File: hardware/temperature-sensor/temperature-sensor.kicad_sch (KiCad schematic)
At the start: 0 parts

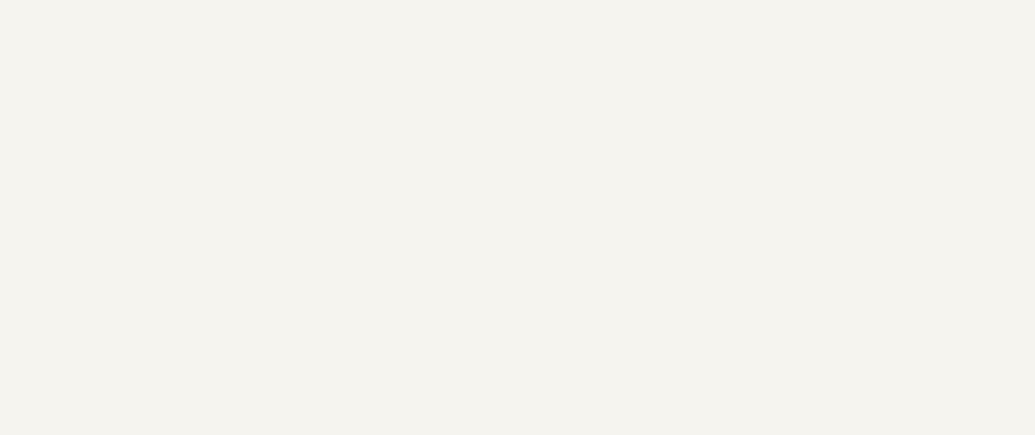
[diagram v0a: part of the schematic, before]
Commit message: extend schematic of ethernet
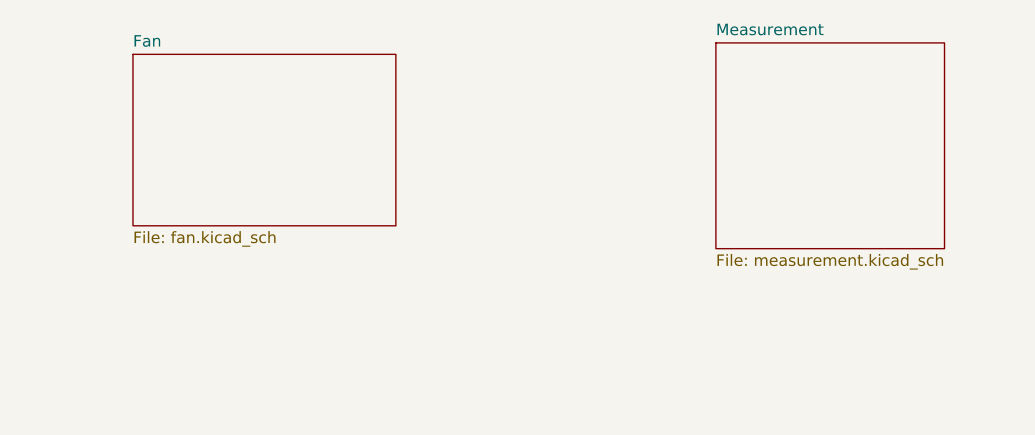
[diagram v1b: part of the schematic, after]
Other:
- added sheet Fan (fan.kicad_sch)
- added sheet Measurement (measurement.kicad_sch)
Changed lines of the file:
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@@
 	(paper "A4")
+	(sheet
+		(at 130.81 53.34)
+		(size 29.21 19.05)
+		(fields_autoplaced yes)
+		(stroke
+			(width 0.1524)
+			(type solid)
+		)
+		(fill
+			(color 0 0 0 0.0000)
+		)
+		(property "Sheetname" "Fan"
+			(at 130.81 52.6284 0)
+			(effects
+				(font
+					(size 1.27 1.27)
+				)
+				(justify left bottom)
+			)
+		)
+		(property "Sheetfile" "fan.kicad_sch"
+			(at 130.81 72.9746 0)
+			(effects
+				(font
+					(size 1.27 1.27)
+				)
+				(justify left top)
+			)
+		)
+		(instances
+			(project "temperature-sensor"
+				(path "/3594a937-0ff5-42e2-8a8f-f816088f7574"
+					(page "4")
+				)
+			)
+		)
+	)
+	(sheet
+		(at 195.58 52.07)
+		(size 25.4 22.86)
+		(fields_autoplaced yes)
+		(stroke
+			(width 0.1524)
+			(type solid)
+		)
+		(fill
+			(color 0 0 0 0.0000)
+		)
+		(property "Sheetname" "Measurement"
+			(at 195.58 51.3584 0)
+			(effects
+				(font
+					(size 1.27 1.27)
+				)
+				(justify left bottom)
+			)
+		)
+		(property "Sheetfile" "measurement.kicad_sch"
+			(at 195.58 75.5146 0)
+			(effects
+				(font
+					(size 1.27 1.27)
+				)
+				(justify left top)
+			)
+		)
+		(instances
+			(project "temperature-sensor"
+				(path "/3594a937-0ff5-42e2-8a8f-f816088f7574"
+					(page "5")
+				)
+			)
+		)
+	)
 	(sheet
 		(at 118.11 106.68)

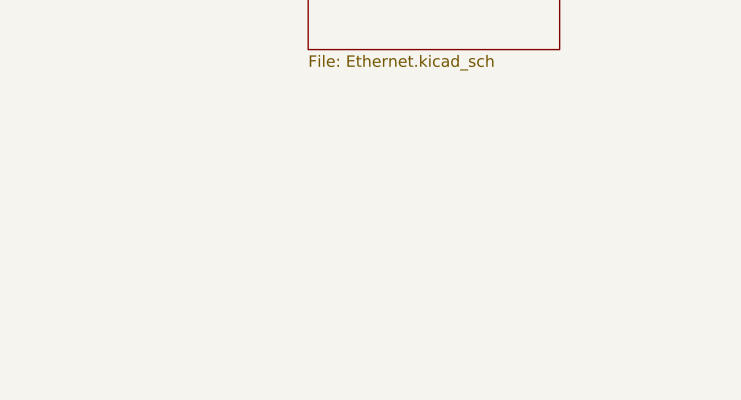
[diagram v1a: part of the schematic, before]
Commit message: replace lan transformer with a 2 channel version
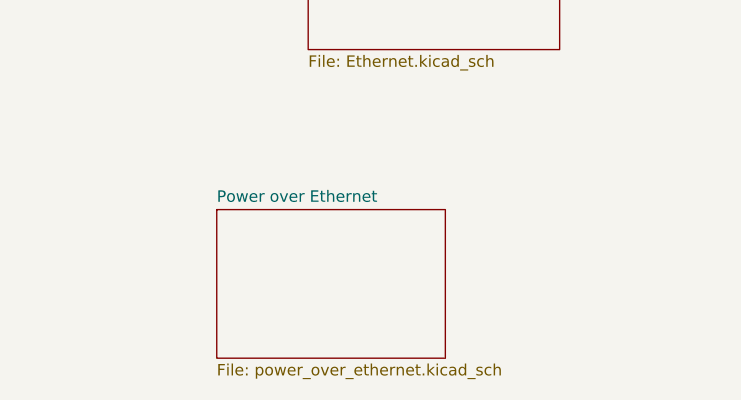
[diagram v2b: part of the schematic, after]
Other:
- added sheet Power over Ethernet (power_over_ethernet.kicad_sch)
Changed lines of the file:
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@@
+	)
+	(sheet
+		(at 172.72 134.62)
+		(size 25.4 16.51)
+		(fields_autoplaced yes)
+		(stroke
+			(width 0.1524)
+			(type solid)
+		)
+		(fill
+			(color 0 0 0 0.0000)
+		)
+		(property "Sheetname" "Power over Ethernet"
+			(at 172.72 133.9084 0)
+			(effects
+				(font
+					(size 1.27 1.27)
+				)
+				(justify left bottom)
+			)
+		)
+		(property "Sheetfile" "power_over_ethernet.kicad_sch"
+			(at 172.72 151.7146 0)
+			(effects
+				(font
+					(size 1.27 1.27)
+				)
+				(justify left top)
+			)
+		)
+		(instances
+			(project "temperature-sensor"
+				(path "/3594a937-0ff5-42e2-8a8f-f816088f7574"
+					(page "6")
+				)
+			)
+		)
 	)
 	(sheet

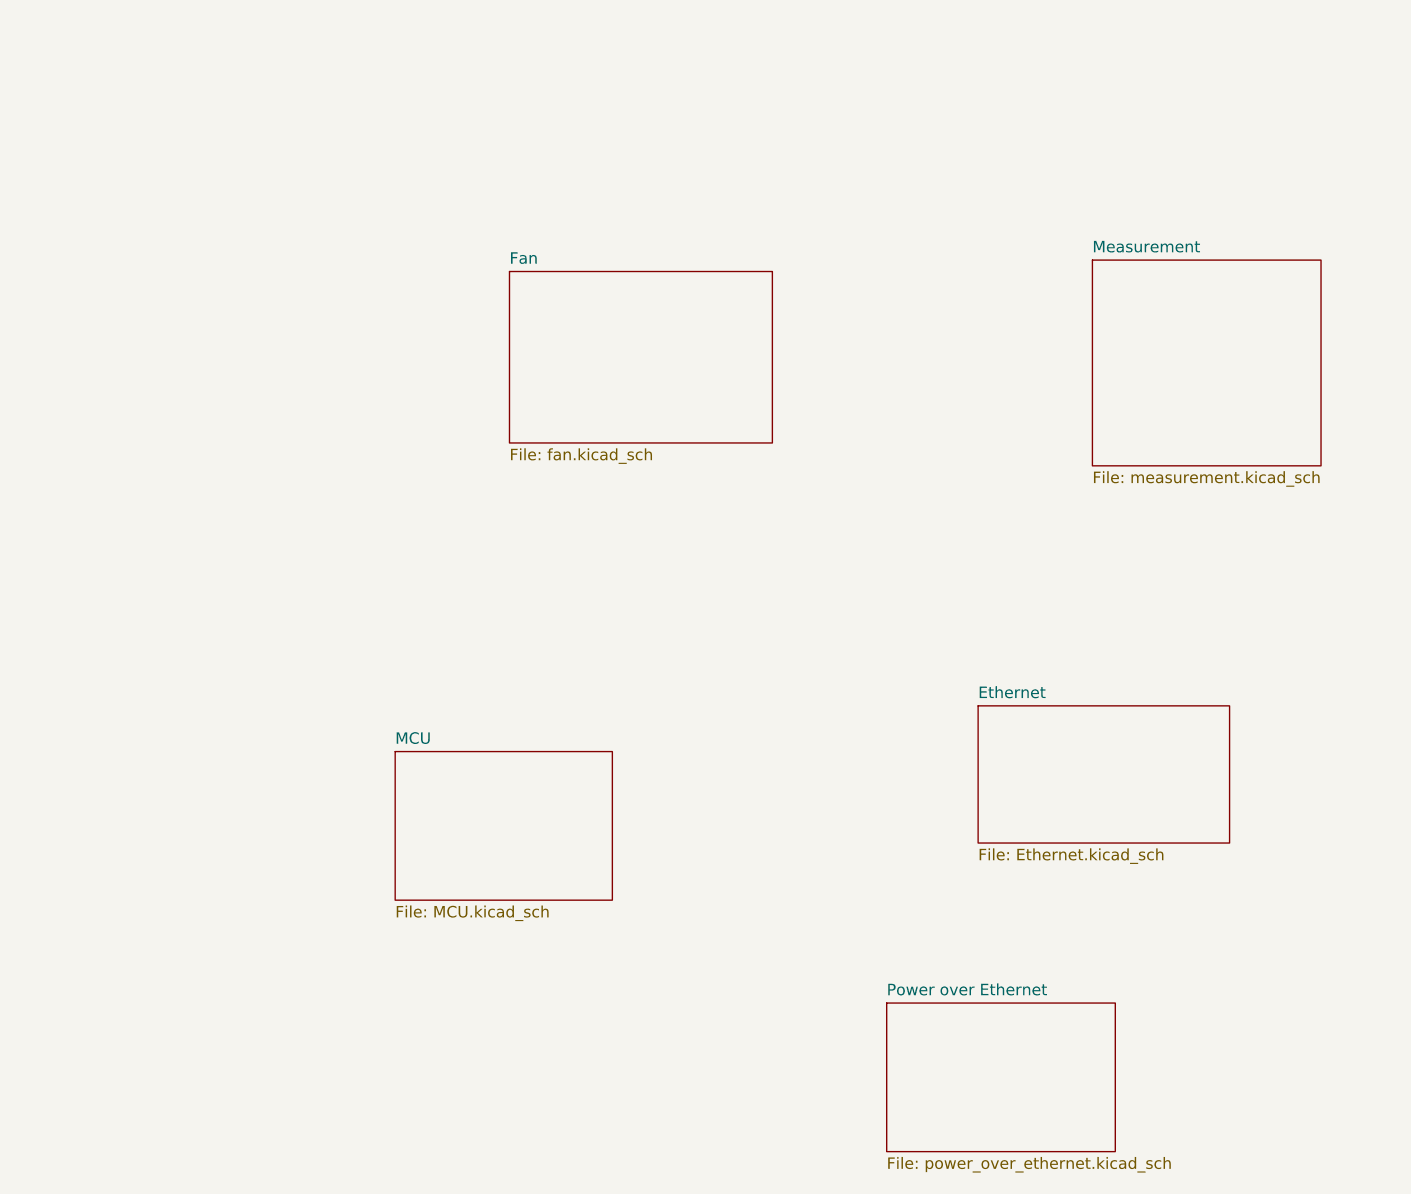
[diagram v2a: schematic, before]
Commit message: work on temperature sensor
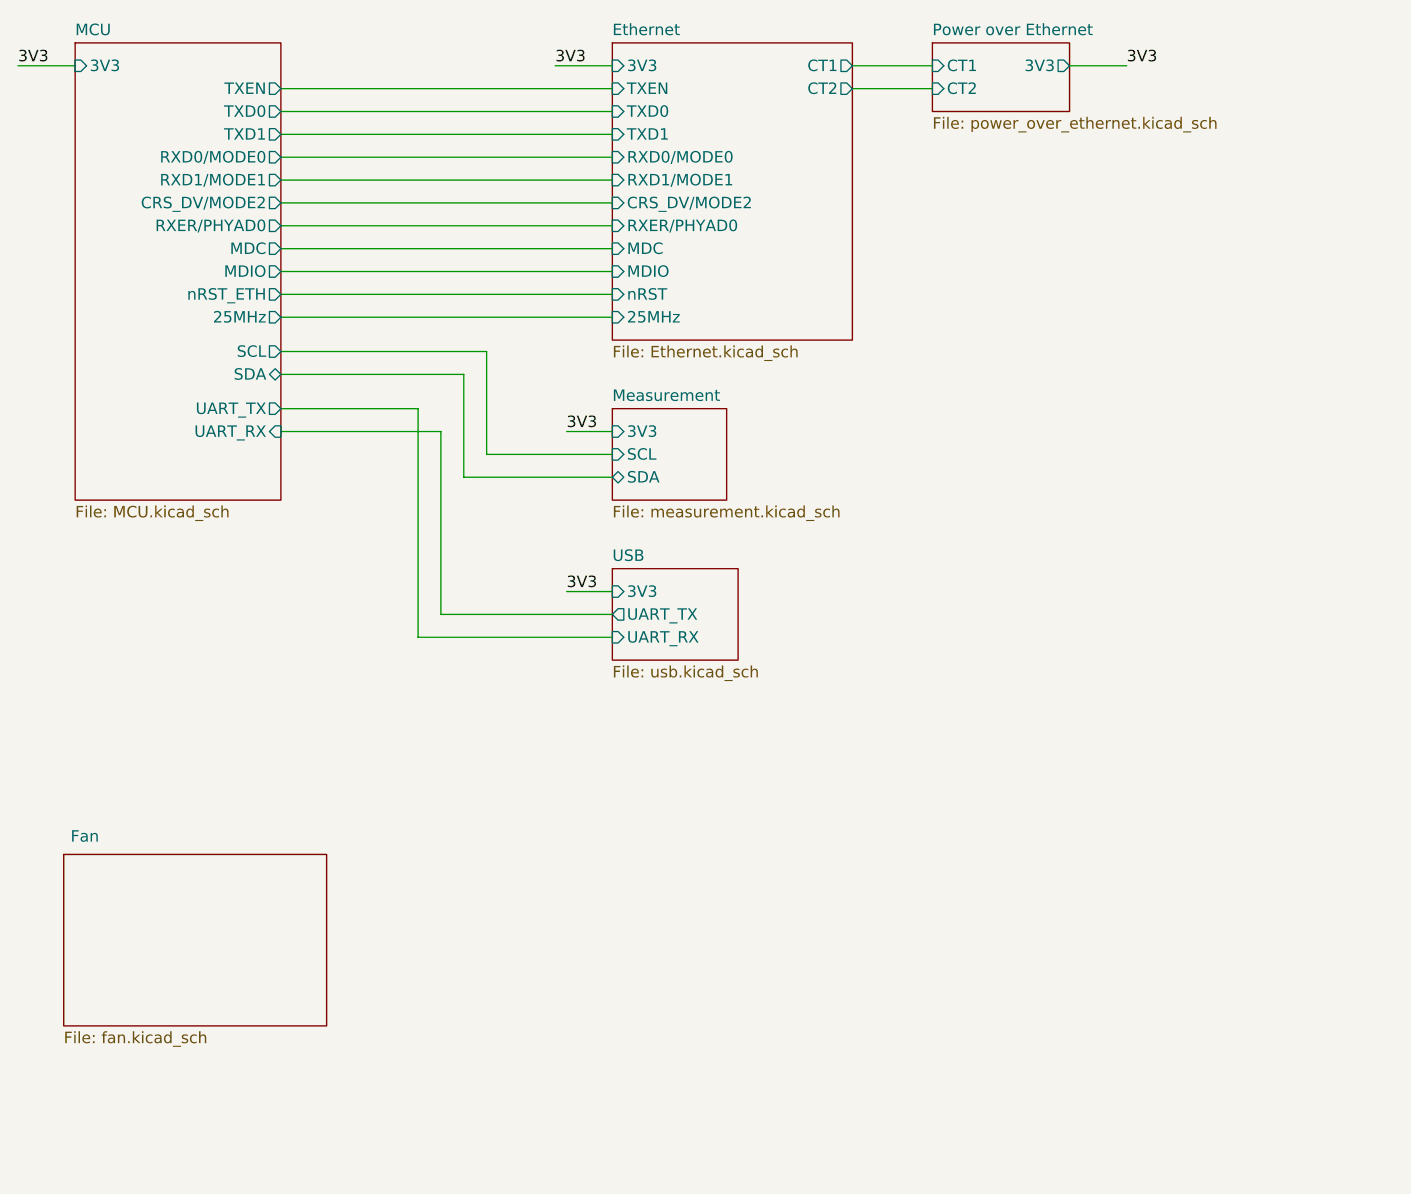
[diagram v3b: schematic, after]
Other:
- added sheet USB (usb.kicad_sch)
- sheet Ethernet ports: added 25MHz, 3V3, CRS_DV/MODE2, CT1, CT2, MDC, MDIO, RXD0/MODE0, RXD1/MODE1, RXER/PHYAD0, TXD0, TXD1, TXEN, nRST; removed none
- sheet MCU ports: added 25MHz, 3V3, CRS_DV/MODE2, MDC, MDIO, RXD0/MODE0, RXD1/MODE1, RXER/PHYAD0, SCL, SDA, TXD0, TXD1, TXEN, UART_RX, UART_TX, nRST_ETH; removed none
- sheet Measurement ports: added 3V3, SCL, SDA; removed none
- sheet Power over Ethernet ports: added 3V3, CT1, CT2; removed none

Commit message: work on temperature sensor
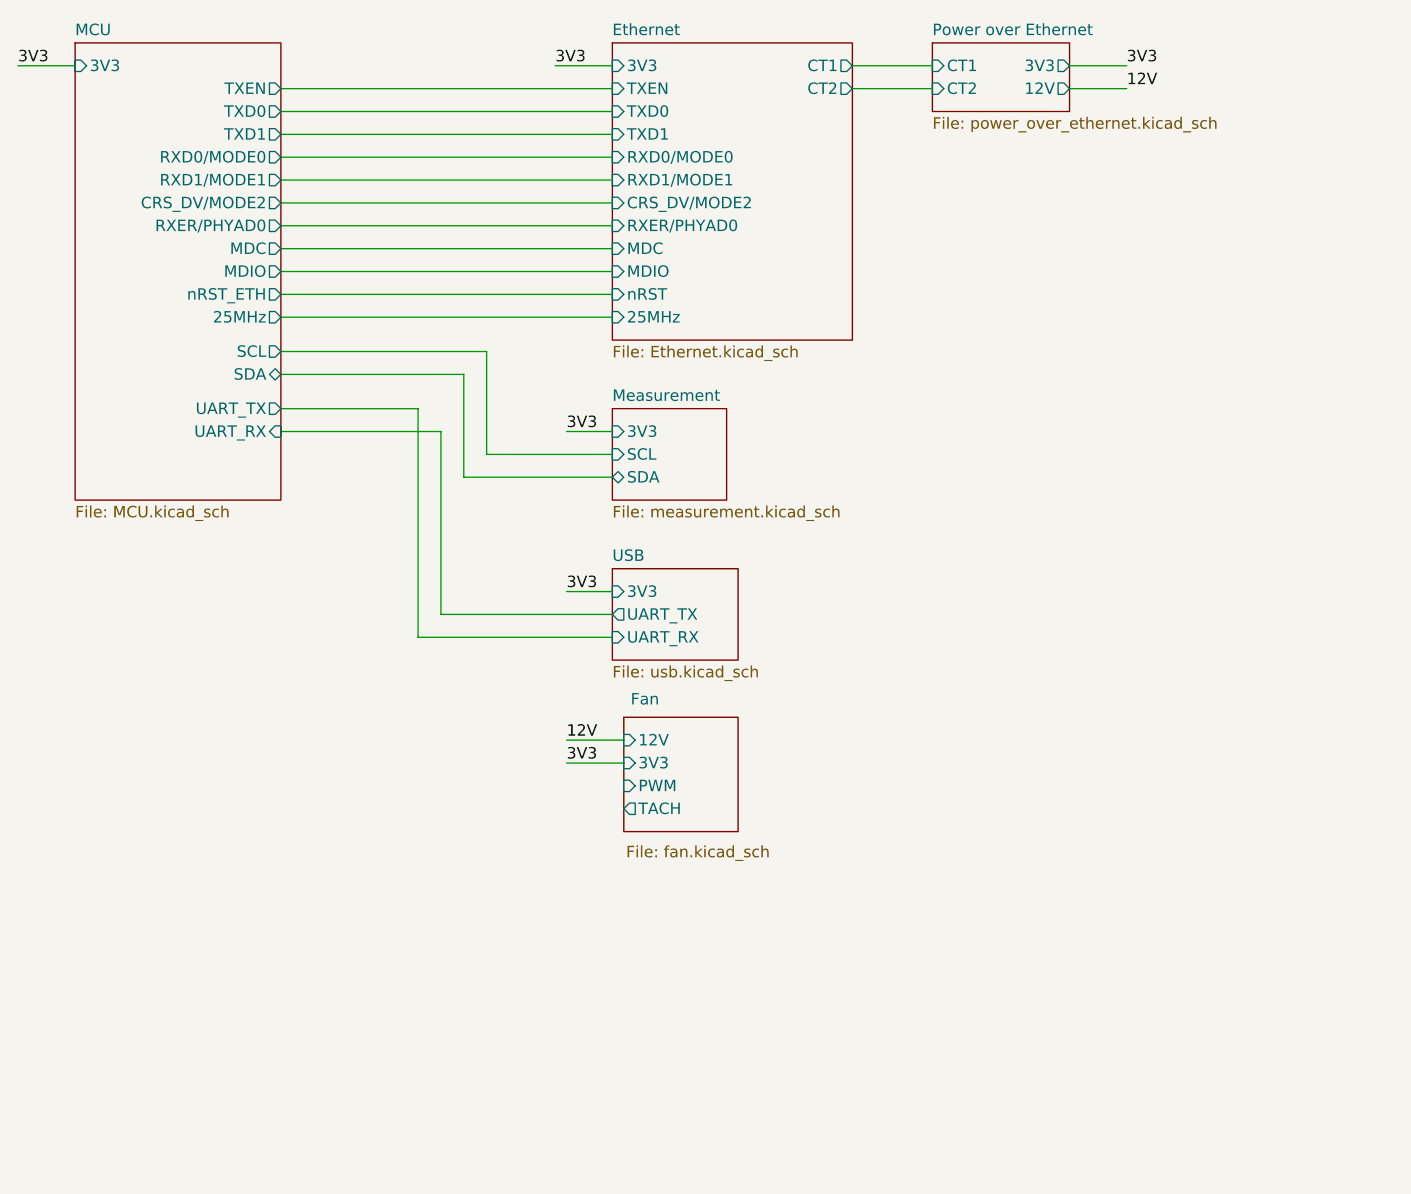
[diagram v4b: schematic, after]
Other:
- sheet Fan ports: added 12V, 3V3, PWM, TACH; removed none
- sheet Power over Ethernet ports: added 12V; removed none
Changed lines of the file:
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@@
+	(wire
+		(pts
+			(xy 137.16 107.95) (xy 143.51 107.95)
+		)
+		(stroke
+			(width 0)
+			(type default)
+		)
+	)
+	(wire
+		(pts
+			(xy 193.04 33.02) (xy 199.39 33.02)
+		)
+		(stroke
+			(width 0)
+			(type default)
+		)
+	)
 	(wire
 		(pts
@@
 		)
 	)
+	(wire
+		(pts
+			(xy 137.16 105.41) (xy 143.51 105.41)
+		)
+		(stroke
+			(width 0)
+			(type default)
+		)
+	)
+	(label "12V"
+		(at 137.16 105.41 0)
+		(effects
+			(font
+				(size 1.27 1.27)
+			)
+			(justify left bottom)
+		)
+	)
 	(label "3V3"
 		(at 137.16 71.12 0)
@@
 		)
 	)
+	(label "12V"
+		(at 199.39 33.02 0)
+		(effects
+			(font
+				(size 1.27 1.27)
+			)
+			(justify left bottom)
+		)
+	)
 	(label "3V3"
 		(at 137.16 88.9 0)
@@
 	)
 	(label "3V3"
+		(at 137.16 107.95 0)
+		(effects
+			(font
+				(size 1.27 1.27)
+			)
+			(justify left bottom)
+		)
+	)
+	(label "3V3"
 		(at 199.39 30.48 0)
 		(effects
@@
 	)
 	(sheet
-		(at 81.28 118.11)
-		(size 29.21 19.05)
+		(at 143.51 102.87)
+		(size 12.7 12.7)
 		(stroke
 			(width 0.1524)
@@
 		)
 		(property "Sheetname" "Fan"
-			(at 82.042 116.84 0)
+			(at 144.272 101.6 0)
 			(effects
 				(font
@@
 		)
 		(property "Sheetfile" "fan.kicad_sch"
-			(at 81.28 137.7446 0)
+			(at 143.764 117.094 0)
 			(effects
 				(font
@@
 				)
 				(justify left top)
+			)
+		)
+		(pin "12V" input
+			(at 143.51 105.41 180)
+			(effects
+				(font
+					(size 1.27 1.27)
+				)
+				(justify left)
+			)
+		)
+		(pin "PWM" input
+			(at 143.51 110.49 180)
+			(effects
+				(font
+					(size 1.27 1.27)
+				)
+				(justify left)
+			)
+		)
+		(pin "TACH" output
+			(at 143.51 113.03 180)
+			(effects
+				(font
+					(size 1.27 1.27)
+				)
+				(justify left)
+			)
+		)
+		(pin "3V3" input
+			(at 143.51 107.95 180)
+			(effects
+				(font
+					(size 1.27 1.27)
+				)
+				(justify left)
 			)
 		)
@@
 			)
 		)
+		(pin "12V" output
+			(at 193.04 33.02 0)
+			(effects
+				(font
+					(size 1.27 1.27)
+				)
+				(justify right)
+			)
+		)
